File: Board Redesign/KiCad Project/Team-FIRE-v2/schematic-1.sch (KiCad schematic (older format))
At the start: 16 parts

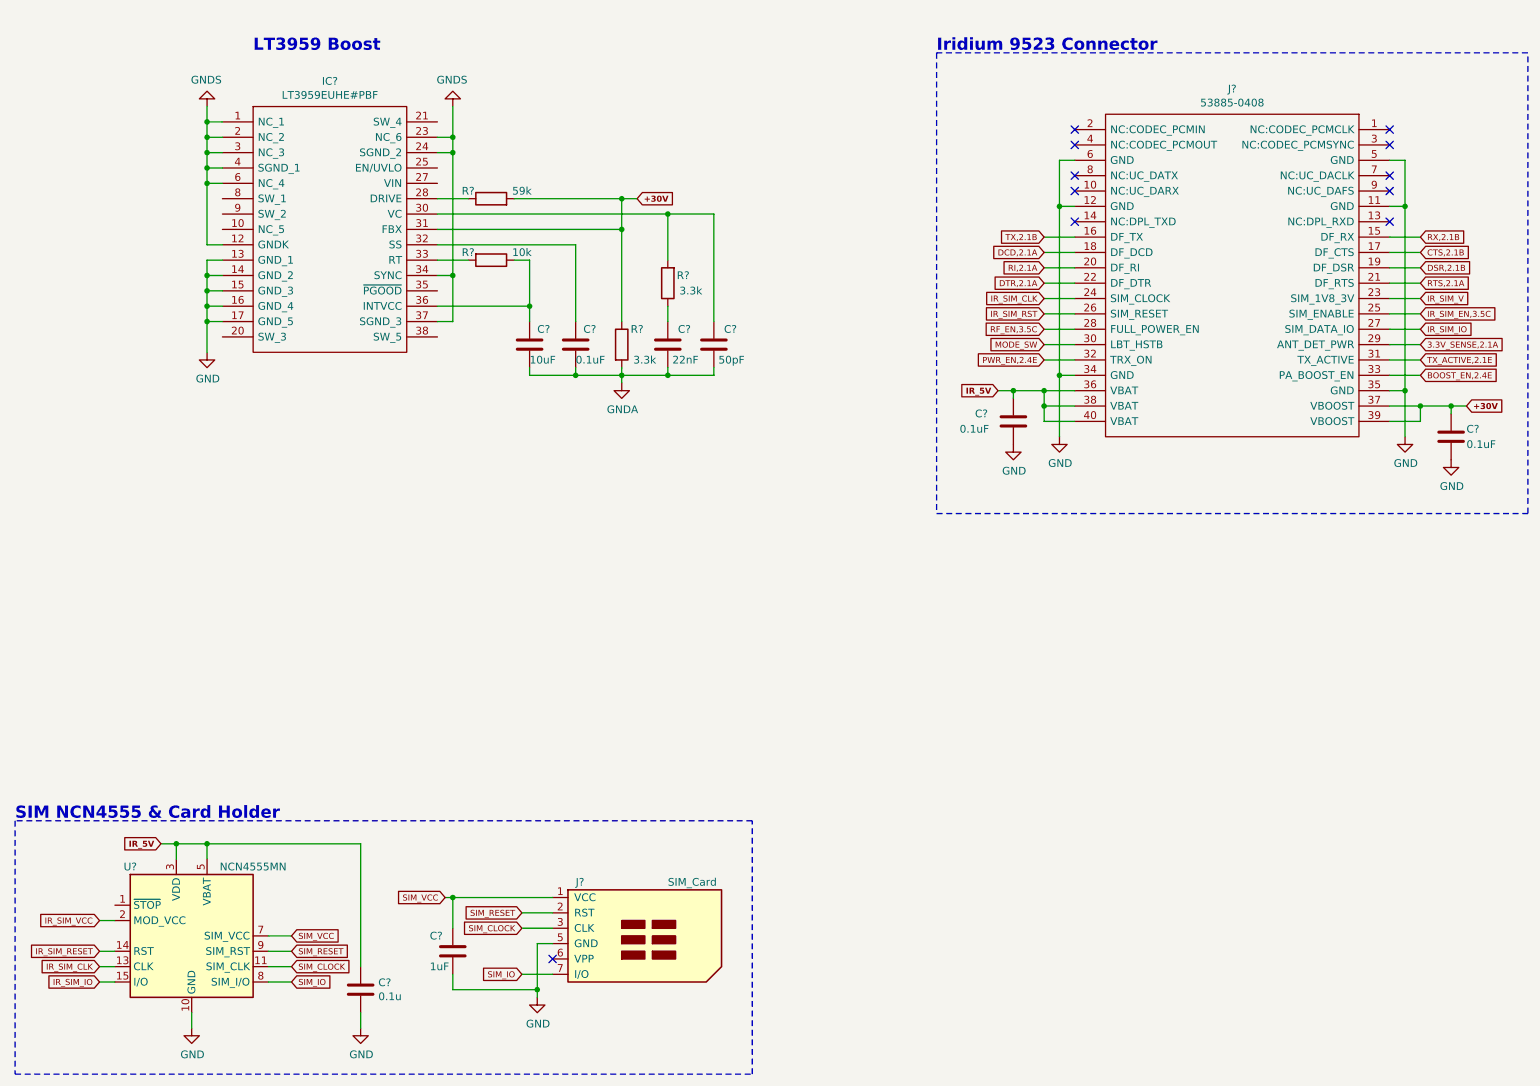
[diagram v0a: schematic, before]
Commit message: Made more progress on board redesign
- Primarily deleted useless (for our purposes) items from the old schematic so we do not have to spend time transferring them over.
- Finished some component transfer
- Renamed some folders
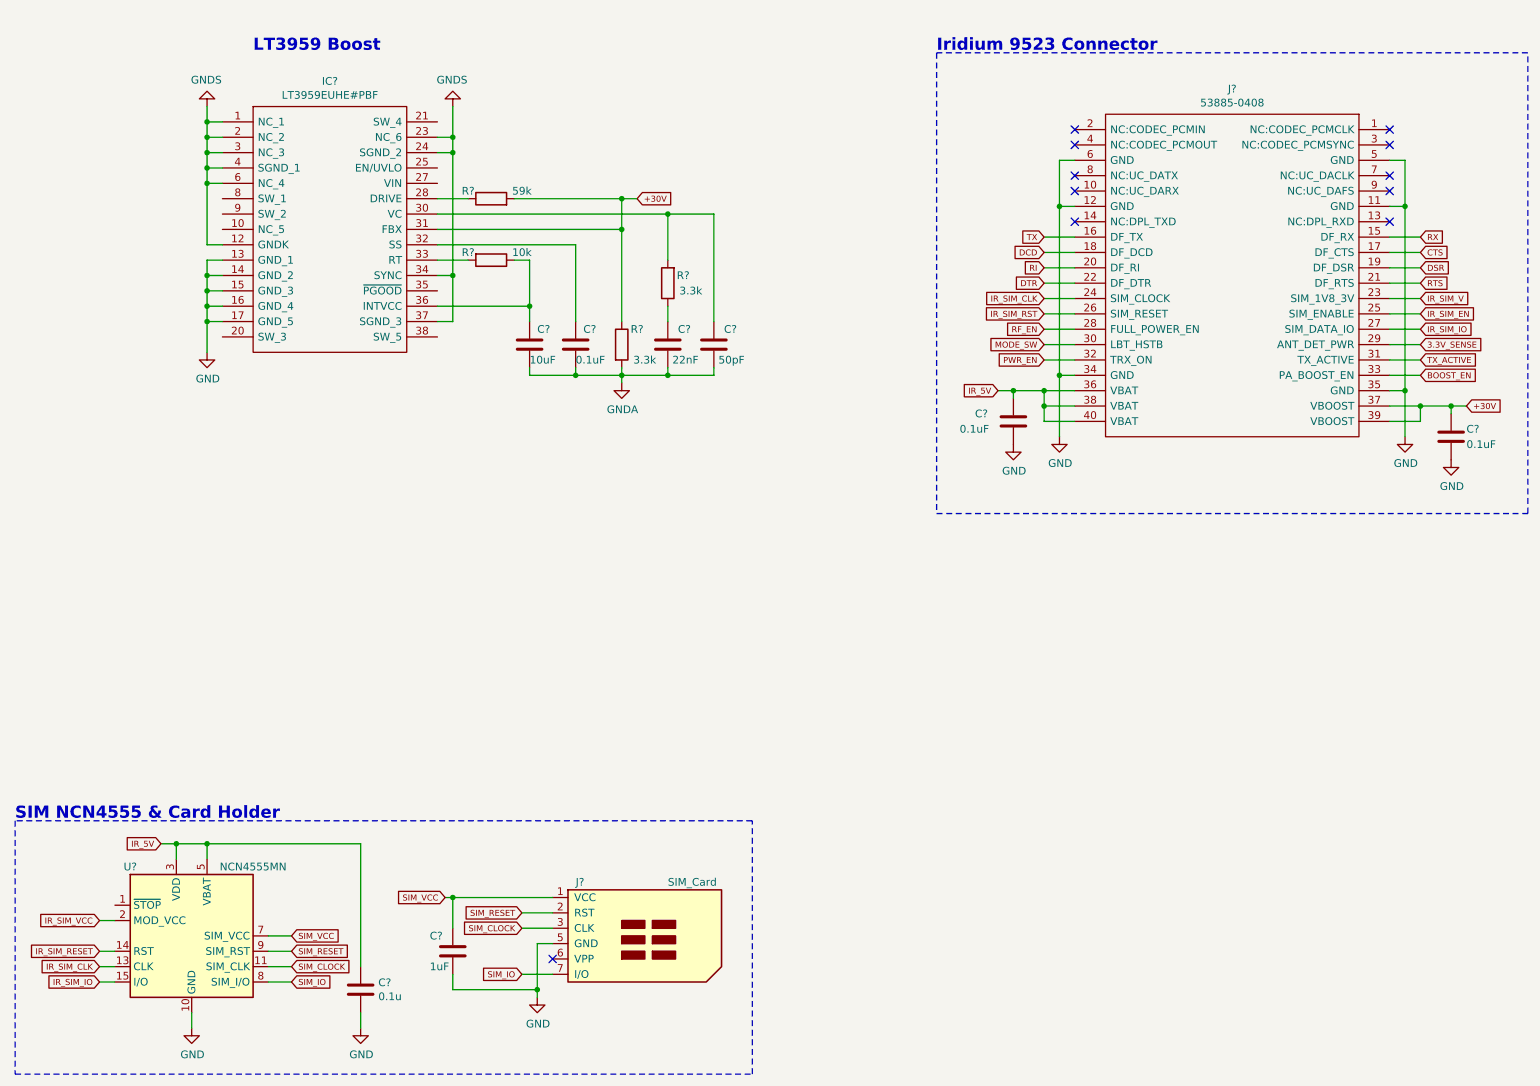
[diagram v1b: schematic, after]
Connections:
- net 3.3V_SENSE,2.1A renamed 3.3V_SENSE
- net BOOST_EN,2.4E renamed BOOST_EN
- net CTS,2.1B renamed CTS
- net DCD,2.1A renamed DCD
- net DSR,2.1B renamed DSR
- net DTR,2.1A renamed DTR
- net IR_SIM_EN,3.5C renamed IR_SIM_EN
- net PWR_EN,2.4E renamed PWR_EN
- net RF_EN,3.5C renamed RF_EN
- net RI,2.1A renamed RI
- net RTS,2.1A renamed RTS
- net RX,2.1B renamed RX
- net TX,2.1B renamed TX
- net TX_ACTIVE,2.1E renamed TX_ACTIVE
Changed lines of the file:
@@
 encoding utf-8
 Sheet 2 3
-Title ""
-Date ""
-Rev ""
-Comp ""
+Title "Team FIRE Board Redesign"
+Date "2020-02-20"
+Rev "v2.0"
+Comp "University of Idaho"
 Comment1 ""
 Comment2 ""
 Comment3 ""
-Comment4 ""
+Comment4 "Koffi Anderson, Collin Heist, Shelby Linafelter"
 $EndDescr
 Text Notes 7000 850  0    79   ~ 16
@@
 	7700 3050 7700 3150
 Connection ~ 7700 3150
-Text GLabel 7400 3050 0    39   Input ~ 8
+Text GLabel 7400 3050 0    39   Input ~ 0
 IR_5V
 $Comp
@@
 MODE_SW
 Text GLabel 7700 2850 0    39   Input ~ 0
-PWR_EN,2.4E
+PWR_EN
 Text GLabel 7700 2650 0    39   Input ~ 0
-RF_EN,3.5C
+RF_EN
 Text GLabel 7700 2550 0    39   Input ~ 0
 IR_SIM_RST
@@
 IR_SIM_CLK
 Text GLabel 7700 2350 0    39   Input ~ 0
-DTR,2.1A
+DTR
 Text GLabel 7700 2250 0    39   Input ~ 0
-RI,2.1A
+RI
 Text GLabel 7700 2150 0    39   Input ~ 0
-DCD,2.1A
+DCD
 Text GLabel 7700 2050 0    39   Input ~ 0
-TX,2.1B
+TX
 Wire Wire Line
 	7900 2650 7700 2650
@@
 NoConn ~ 9950 1350
 Text GLabel 10150 2050 2    39   Input ~ 0
-RX,2.1B
+RX
 Text GLabel 10150 2150 2    39   Input ~ 0
-CTS,2.1B
+CTS
 Text GLabel 10150 2250 2    39   Input ~ 0
-DSR,2.1B
+DSR
 Text GLabel 10150 2350 2    39   Input ~ 0
-RTS,2.1A
+RTS
 Text GLabel 10150 2450 2    39   Input ~ 0
 IR_SIM_V
 Text GLabel 10150 2550 2    39   Input ~ 0
-IR_SIM_EN,3.5C
+IR_SIM_EN
 Text GLabel 10150 2650 2    39   Input ~ 0
 IR_SIM_IO
 Text GLabel 10150 2750 2    39   Input ~ 0
-3.3V_SENSE,2.1A
+3.3V_SENSE
 Text GLabel 10150 2850 2    39   Input ~ 0
-TX_ACTIVE,2.1E
+TX_ACTIVE
 Text GLabel 10150 2950 2    39   Input ~ 0
-BOOST_EN,2.4E
+BOOST_EN
 Wire Wire Line
 	9950 2050 10150 2050
@@
 	10350 3150 10450 3150
 Connection ~ 10350 3150
-Text GLabel 10450 3150 2    39   Input ~ 8
+Text GLabel 10450 3150 2    39   Input ~ 0
 +30V
 Wire Notes Line
@@
 Wire Wire Line
 	2050 6000 2250 6000
-Text GLabel 1950 6000 0    39   Input ~ 8
+Text GLabel 1950 6000 0    39   Input ~ 0
 IR_5V
 Connection ~ 2050 6000
@@
 	4950 1800 5050 1800
 Connection ~ 4950 1800
-Text GLabel 5050 1800 2    39   Input ~ 8
+Text GLabel 5050 1800 2    39   Input ~ 0
 +30V
 $EndSCHEMATC

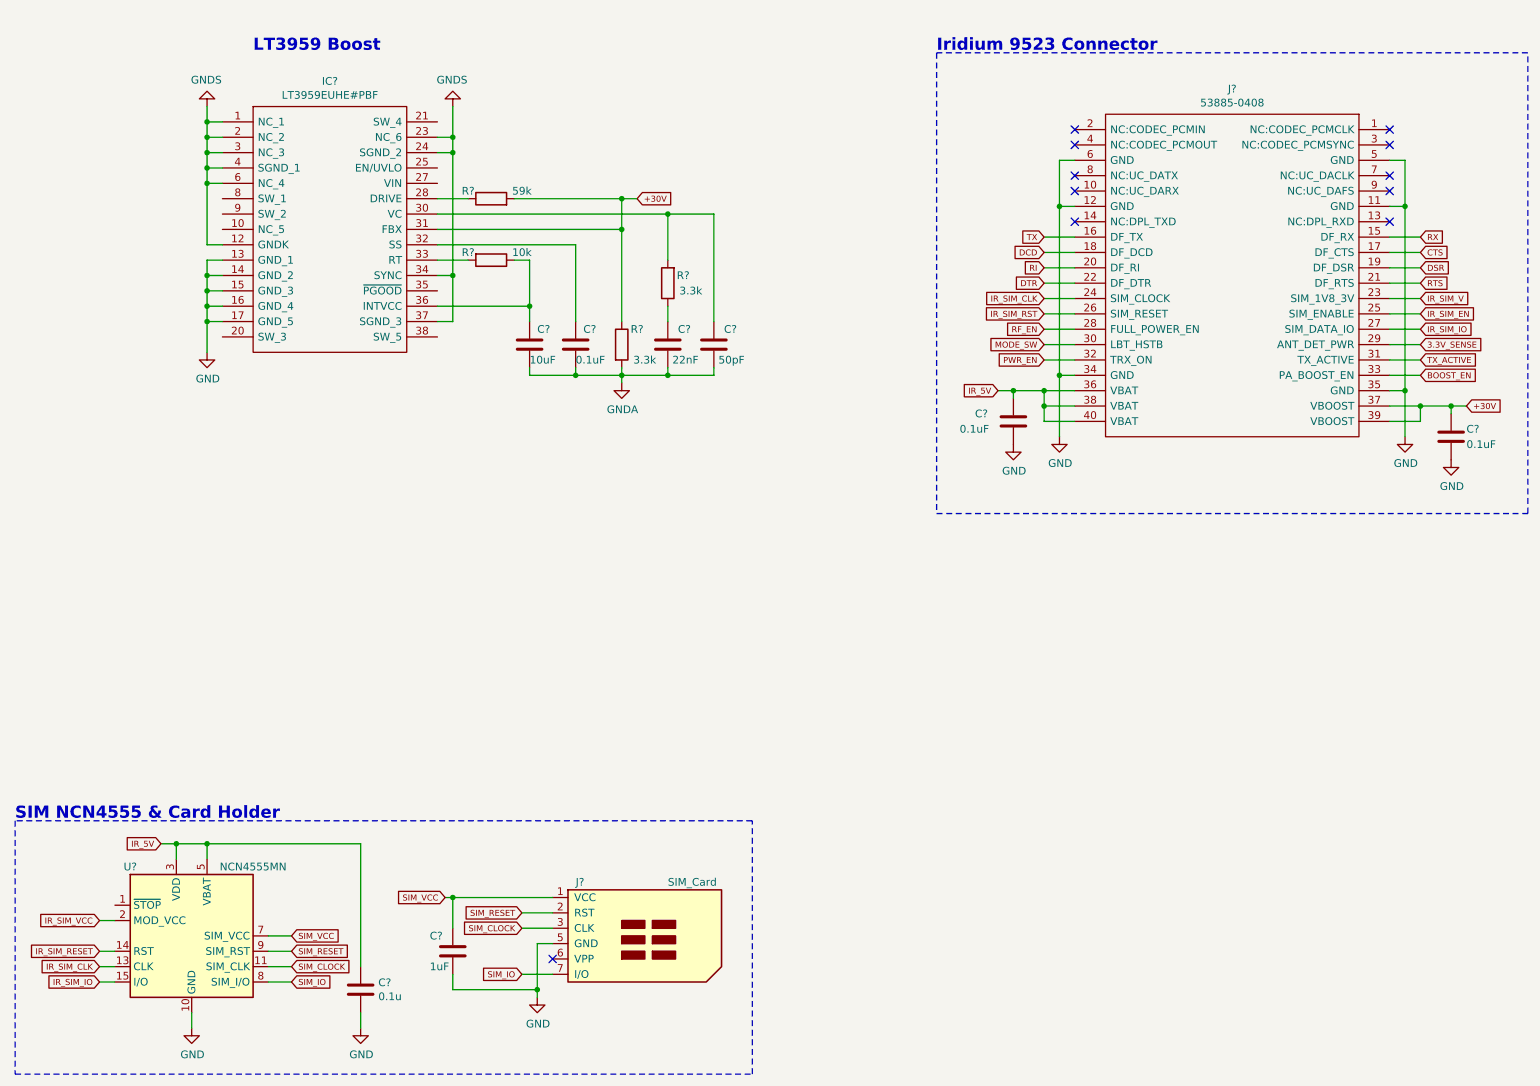
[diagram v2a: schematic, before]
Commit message: Added changes to SCH1
- Added Shelby's changes to SCH1
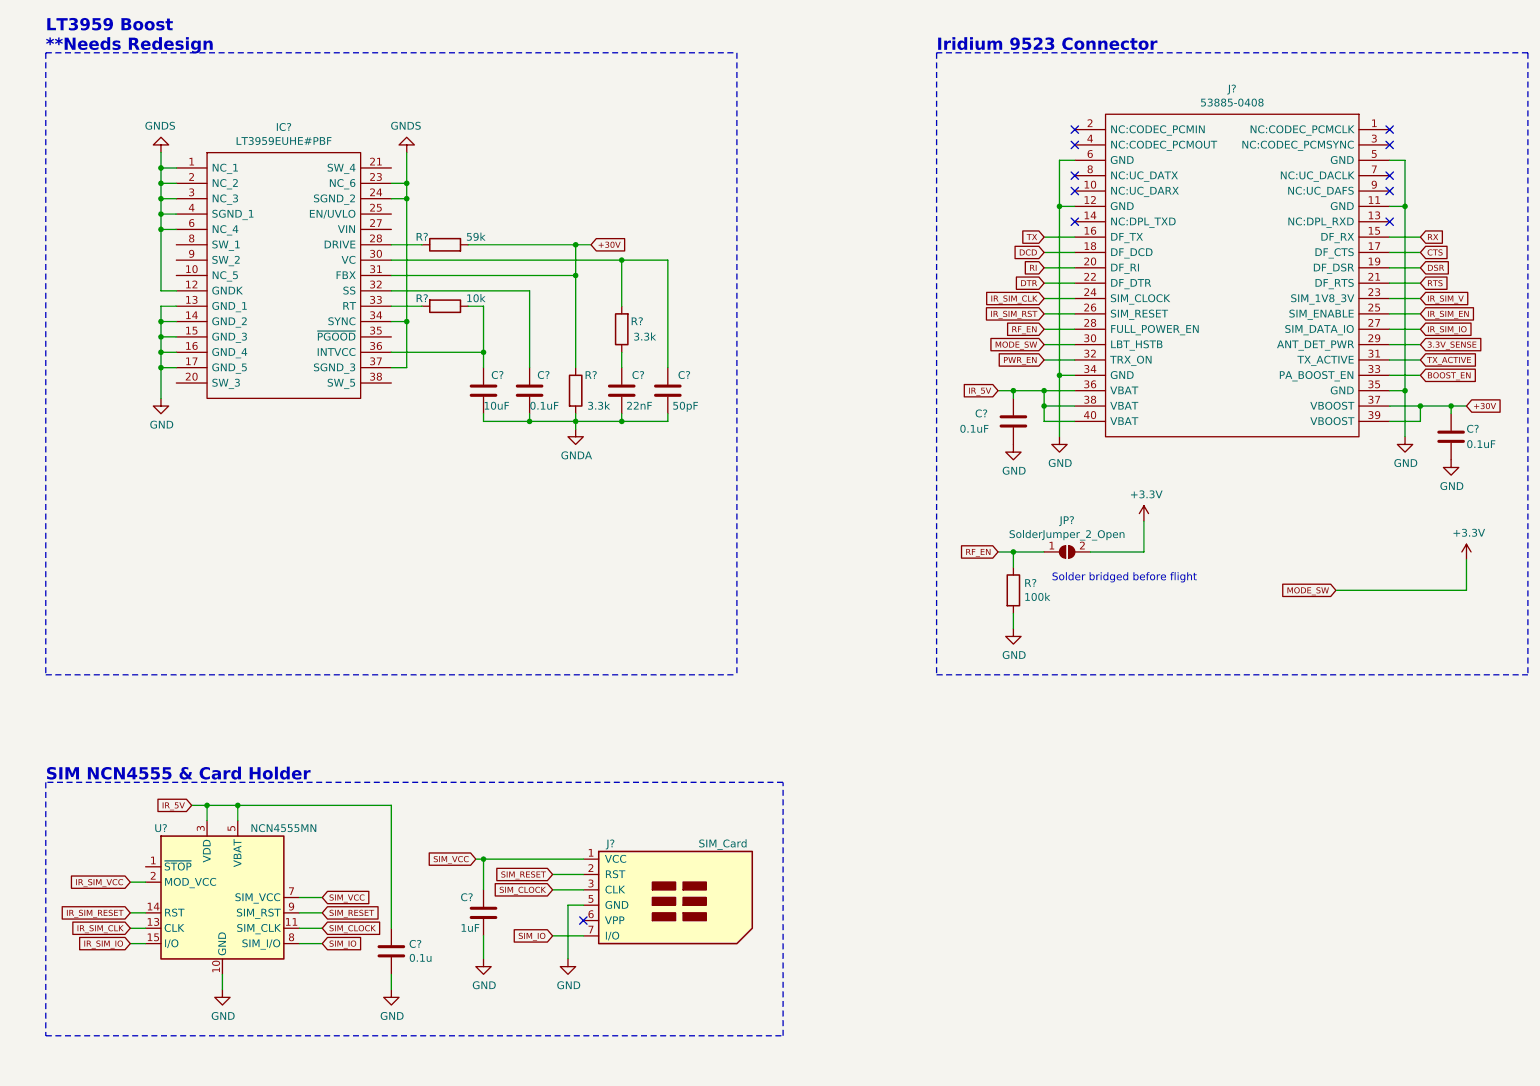
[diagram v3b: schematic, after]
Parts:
- added JP?: SolderJumper_2_Open, symbol Jumper:SolderJumper_2_Open
- added R?: 100k, symbol Device:R
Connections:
- net GND: now also R?.2
- net RF_EN: now also JP?.1 (A), R?.1
- net MODE_SW renamed +3V3
- net +3V3: now also JP?.2 (B)
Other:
- note added: "LT3959 Boost\n**Needs Redesign"
- note added: "Solder bridged before flight"
- note removed: "LT3959 Boost"
- moved on the sheet: C?, IC?, J?, R?, U?

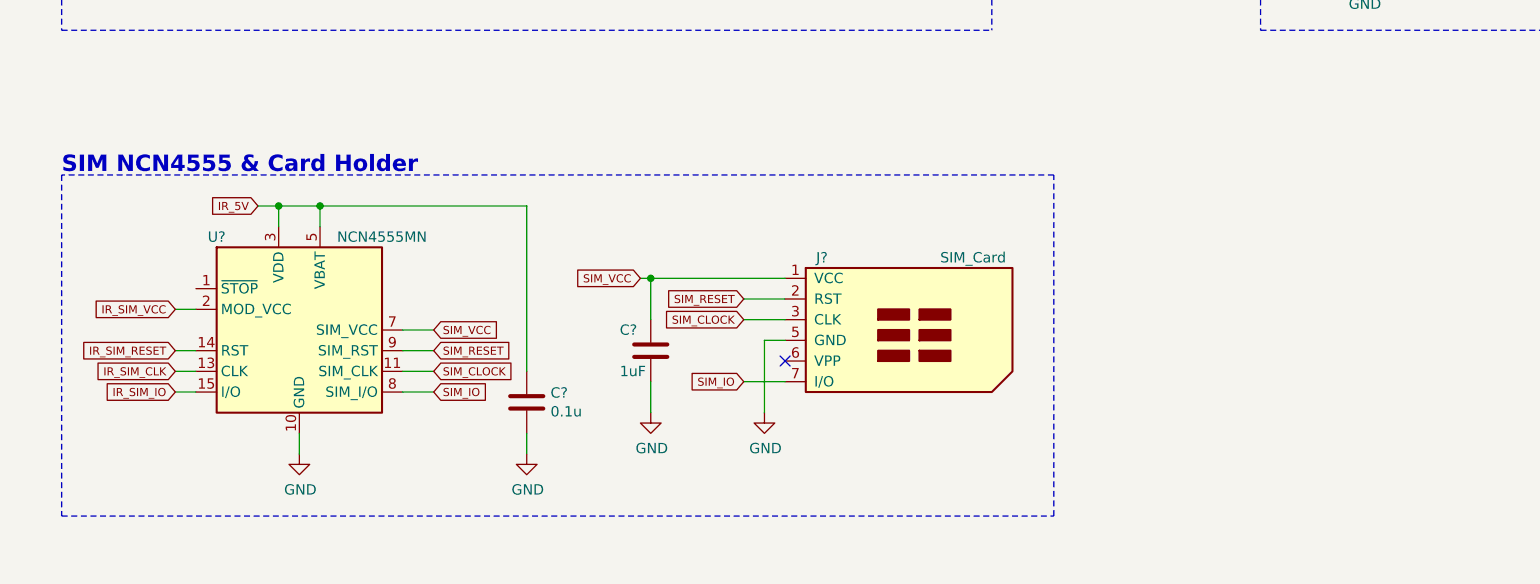
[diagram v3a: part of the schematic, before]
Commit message: Added SAMD51
- Created schematic symbol, footprint, and 3D model for the SAMD51
- Added SAMD51 to the schematic (only partially implemented)
- Added decoupling capacitors to the 3.3V bus (as recommended by the SAMD51 design manual)
- Started checklist for SAMD51 implementation on the top-level schematic sheet; there's no convenient breakout board to emulate
- Implemented power connections for SAMD51
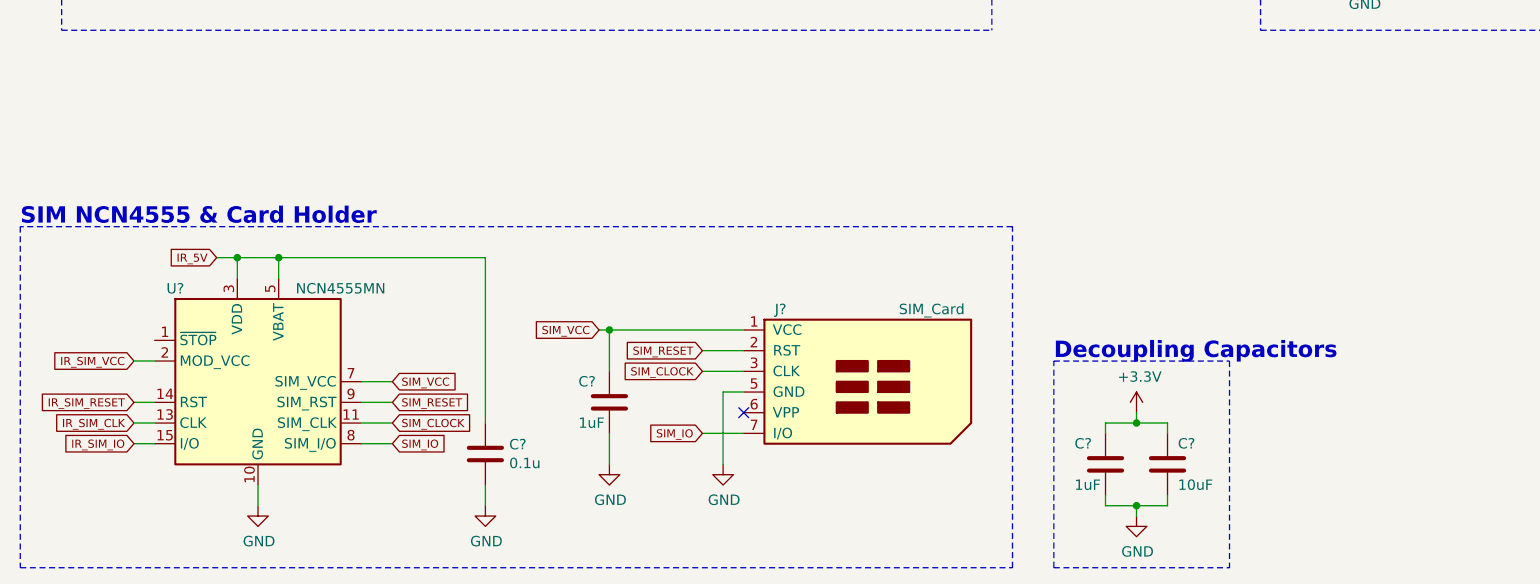
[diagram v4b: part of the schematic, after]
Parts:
- added C?: 1uF, Inductor_SMD:L_0603_1608Metric, symbol Device:C
- added C?: 10uF, Inductor_SMD:L_0603_1608Metric, symbol Device:C
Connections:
- net +3V3: now also C?.1, C?.1
- net GND: now also C?.2, C?.2
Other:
- note added: "Decoupling Capacitors"
- moved on the sheet: C?, J?, U?

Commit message: Add: no connection flag for (NC) no connect
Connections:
- net GNDS: no longer IC?.1 (NC_1), IC?.2 (NC_2), IC?.23 (NC_6), IC?.3 (NC_3), IC?.6 (NC_4)
- no-connect marks 11 -> 17
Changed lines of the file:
@@
 Text Notes 1200 850  0    79   ~ 16
 LT3959 Boost\n**Needs Redesign
-Wire Wire Line
-	2050 1600 1950 1600
-Wire Wire Line
-	1950 1600 1950 1700
-Wire Wire Line
-	1950 1700 2050 1700
-Wire Wire Line
-	1950 1700 1950 1800
-Wire Wire Line
-	1950 1800 2050 1800
-Connection ~ 1950 1700
-Wire Wire Line
-	1950 1800 1950 1900
-Wire Wire Line
-	1950 1900 2050 1900
-Connection ~ 1950 1800
-Wire Wire Line
-	2050 2000 1950 2000
-Wire Wire Line
-	1950 2000 1950 1900
-Connection ~ 1950 1900
 $Comp
 L power:GNDS #PWR?
@@
 $EndComp
 Wire Wire Line
-	1950 1500 1950 1600
-Connection ~ 1950 1600
-Wire Wire Line
 	3450 2900 3550 2900
 Wire Wire Line
@@
 Wire Wire Line
 	3550 1800 3450 1800
-Wire Wire Line
-	3450 1700 3550 1700
-Wire Wire Line
-	3550 1700 3550 1800
 Connection ~ 3550 1800
 Wire Wire Line
@@
 $EndComp
 Wire Wire Line
-	3550 1500 3550 1700
-Connection ~ 3550 1700
-Wire Wire Line
-	1950 2000 1950 2400
-Wire Wire Line
 	1950 2400 2050 2400
-Connection ~ 1950 2000
 $Comp
 L power:GND #PWR?
@@
 Wire Notes Line
 	6000 7500 6850 7500
+NoConn ~ 2050 1600
+NoConn ~ 2050 1700
+NoConn ~ 2050 1800
+NoConn ~ 2050 2000
+NoConn ~ 2050 2300
+Wire Wire Line
+	3550 1500 3550 1800
+NoConn ~ 3450 1700
+Wire Wire Line
+	2050 1900 1950 1900
+Wire Wire Line
+	1950 1900 1950 1500
+Wire Wire Line
+	1950 1900 1950 2400
+Connection ~ 1950 1900
 $EndSCHEMATC
